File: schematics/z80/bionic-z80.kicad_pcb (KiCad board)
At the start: 2 copper layers, 27.9 x 68.6 mm, 8 parts, among them J1 Bionic-P135, J2 Bionic-P245, U1 Z84C00, U2 11AA010-I/TT

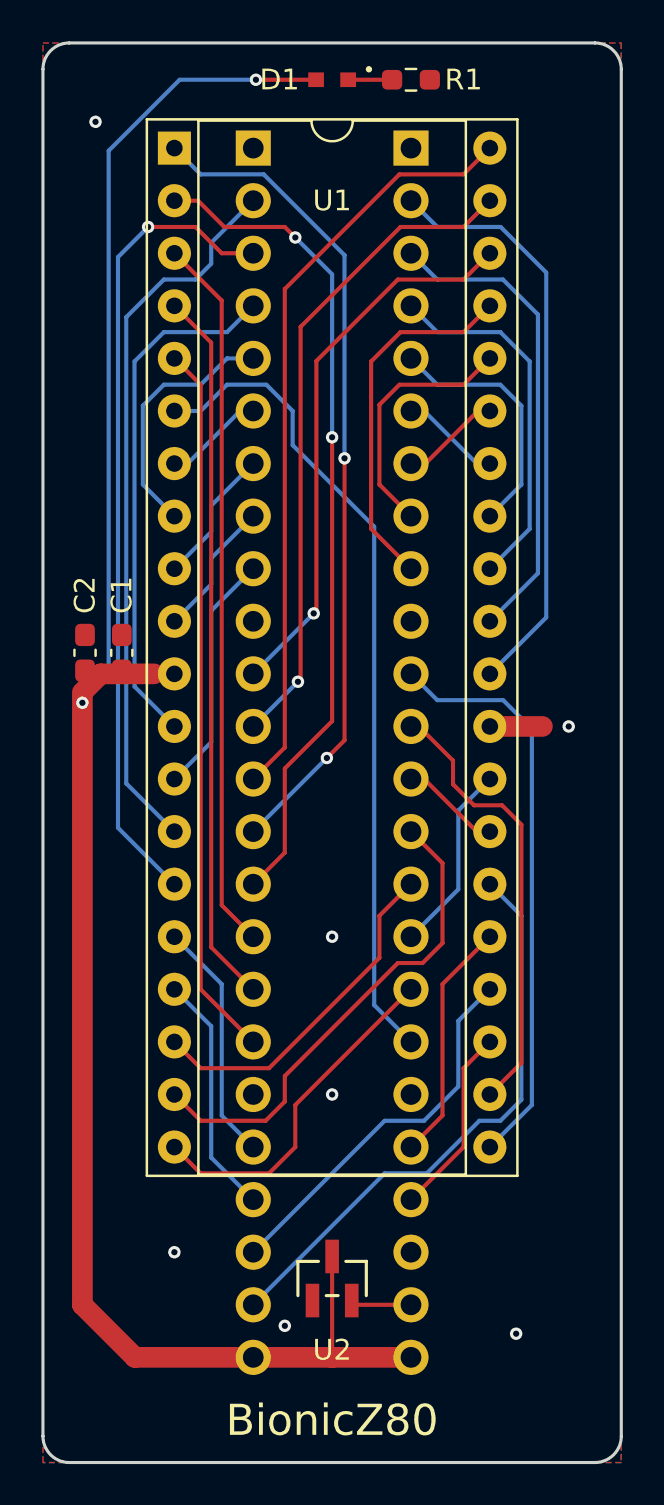
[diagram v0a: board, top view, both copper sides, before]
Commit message: [Z80] Fix EEPROM pinout
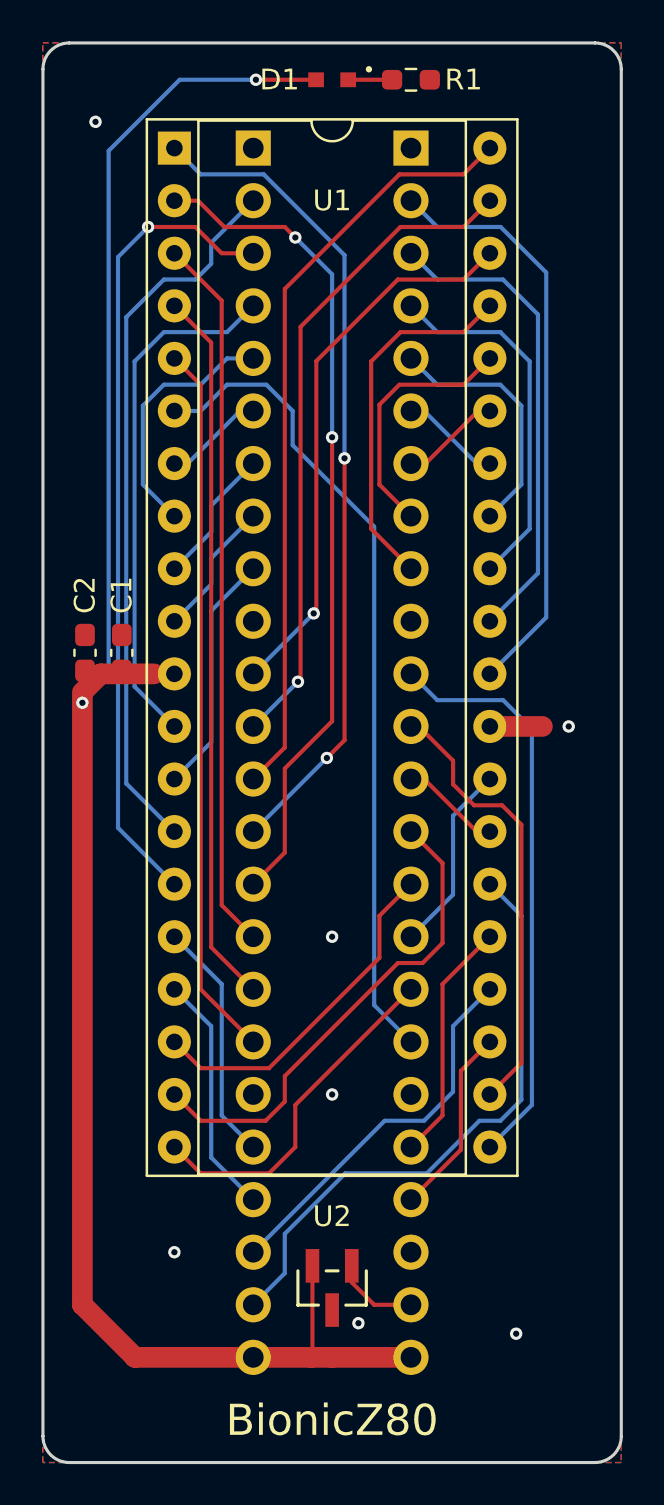
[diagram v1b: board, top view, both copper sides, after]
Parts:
- moved U2 0.46 mm to (115.0, 130.1), turned to 180 degrees
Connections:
- U2 pad 1: GND -> Net-(J2-P57)
- U2 pad 2: Net-(J2-P57) -> VCC
- U2 pad 3: VCC -> GND
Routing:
- net Net-(J2-P57): track 2.66 -> 4.10 mm
- net /P53: track 28.1 -> 29.2 mm
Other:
- board text added: "Rev. 3"
- board text removed: "Rev. 2"
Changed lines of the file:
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@@
   (title_block
     (title "BionicZ80")
-    (date "2024-05-25")
-    (rev "2")
+    (date "2024-11-02")
+    (rev "3")
     (company "Tadashi G. Takaoka")
   )
@@
   )
   (footprint "0-LocalLibrary:SOT-23_MC_MCH-M" (layer "F.Cu")
-    (at 114.97 129.69)
+    (at 114.97 130.148 180)
     (descr "Microchip 11AAxxx-I/TT UNI/O 1Kbit Serial EEPROM")
     (property "Sheetfile" "bionic-z80.kicad_sch")
@@
         (effects (font (size 1 1) (thickness 0.15)))
     )
-    (fp_text value "11AA010-I/TT" (at 0 0 unlocked) (layer "F.Fab")
+    (fp_text value "11AA010-I/TT" (at 0 0 180 unlocked) (layer "F.Fab")
         (effects (font (size 1 1) (thickness 0.15)))
     )
-    (fp_text user "${REFERENCE}" (at 0 0 unlocked) (layer "F.Fab")
+    (fp_text user "${REFERENCE}" (at 0 0 180 unlocked) (layer "F.Fab")
         (effects (font (size 1 1) (thickness 0.15)))
     )
@@
     (fp_circle (center -1.270999 0.446) (end -1.143999 0.446)
       (stroke (width 0.0254) (type solid)) (fill none) (layer "F.Fab"))
-    (pad "1" smd rect (at -0.950001 1.066) (size 0.6604 1.6256) (layers "F.Cu" "F.Paste" "F.Mask")
+    (pad "1" smd rect (at -0.950001 1.066 180) (size 0.6604 1.6256) (layers "F.Cu" "F.Paste" "F.Mask")
+      (net 44 "Net-(J2-P57)") (pinfunction "SCIO") (pintype "bidirectional"))
+    (pad "2" smd rect (at 0.950001 1.066 180) (size 0.6604 1.6256) (layers "F.Cu" "F.Paste" "F.Mask")
+      (net 1 "VCC") (pinfunction "VCC") (pintype "power_in"))
+    (pad "3" smd rect (at 0 -1.066 180) (size 0.6604 1.6256) (layers "F.Cu" "F.Paste" "F.Mask")
       (net 2 "GND") (pinfunction "VSS") (pintype "power_in"))
-    (pad "2" smd rect (at 0.950001 1.066) (size 0.6604 1.6256) (layers "F.Cu" "F.Paste" "F.Mask")
-      (net 44 "Net-(J2-P57)") (pinfunction "SCIO") (pintype "bidirectional"))
-    (pad "3" smd rect (at 0 -1.066) (size 0.6604 1.6256) (layers "F.Cu" "F.Paste" "F.Mask")
-      (net 1 "VCC") (pinfunction "VCC") (pintype "power_in"))
     (model "${KIPRJMOD}/0-LocalLibrary/SOT-23_MC_MCH.step"
       (offset (xyz 0 0 0))
@@
     (effects (font (size 0.8 0.8)) (justify bottom mirror))
   )
-  (gr_text "Rev. 2" (at 107.096 137.437) (layer "B.SilkS")
+  (gr_text "Rev. 3" (at 107.096 137.437) (layer "B.SilkS")
     (effects (font (size 1 1)) (justify left bottom mirror))
   )
@@
   )
   (segment (start 114.1953 71.778) (end 111.287 71.778) (width 0.2) (layer "F.Cu") (net 1))
-  (segment locked (start 114.97 133.5) (end 114.97 128.624) (width 0.2) (layer "F.Cu") (net 1))
-  (segment locked (start 114.97 133.5) (end 111.16 133.5) (width 1) (layer "F.Cu") (net 1))
+  (segment (start 114.019999 133.434001) (end 113.954 133.5) (width 0.2) (layer "F.Cu") (net 1))
   (segment locked (start 103.794 100.48) (end 104.9635 100.48) (width 1) (layer "F.Cu") (net 1))
   (segment locked (start 104.9635 100.48) (end 106.368 100.48) (width 1) (layer "F.Cu") (net 1))
   (segment locked (start 102.905 130.96) (end 102.905 101.369) (width 1) (layer "F.Cu") (net 1))
+  (segment (start 114.019999 129.082) (end 114.019999 133.434001) (width 0.2) (layer "F.Cu") (net 1))
   (segment locked (start 103.032 101.242) (end 103.794 100.48) (width 1) (layer "F.Cu") (net 1))
+  (segment (start 114.97 133.5) (end 113.954 133.5) (width 1) (layer "F.Cu") (net 1))
   (segment locked (start 105.445 133.5) (end 102.905 130.96) (width 1) (layer "F.Cu") (net 1))
   (segment locked (start 118.78 133.5) (end 114.97 133.5) (width 1) (layer "F.Cu") (net 1))
   (segment locked (start 111.16 133.5) (end 105.445 133.5) (width 1) (layer "F.Cu") (net 1))
+  (segment (start 113.954 133.5) (end 111.16 133.5) (width 1) (layer "F.Cu") (net 1))
   (via (at 111.287 71.778) (size 0.6) (drill 0.3) (layers "F.Cu" "B.Cu") (net 1))
   (via (at 102.905 101.877) (size 0.6) (drill 0.3) (layers "F.Cu" "B.Cu") (net 1))
@@
   (via (at 114.97 113.18) (size 0.6) (drill 0.3) (layers "F.Cu" "B.Cu") (free) (net 2))
   (via (at 123.86 132.357) (size 0.6) (drill 0.3) (layers "F.Cu" "B.Cu") (free) (net 2))
-  (via (at 112.684 131.976) (size 0.6) (drill 0.3) (layers "F.Cu" "B.Cu") (free) (net 2))
+  (via (at 116.24 131.849) (size 0.6) (drill 0.3) (layers "F.Cu" "B.Cu") (free) (net 2))
   (via (at 107.35 128.42) (size 0.6) (drill 0.3) (layers "F.Cu" "B.Cu") (free) (net 2))
+  (segment (start 124.114 112.164) (end 122.59 110.64) (width 0.2) (layer "B.Cu") (net 3))
+  (segment (start 115.605 124.61) (end 119.542 124.61) (width 0.2) (layer "B.Cu") (net 3))
+  (segment (start 111.16 130.96) (end 112.684 129.436) (width 0.2) (layer "B.Cu") (net 3))
+  (segment (start 112.684 129.436) (end 112.684 127.531) (width 0.2) (layer "B.Cu") (net 3))
+  (segment (start 123.098 122.07) (end 124.114 121.054) (width 0.2) (layer "B.Cu") (net 3))
+  (segment (start 119.542 124.61) (end 122.082 122.07) (width 0.2) (layer "B.Cu") (net 3))
+  (segment (start 122.082 122.07) (end 123.098 122.07) (width 0.2) (layer "B.Cu") (net 3))
   (segment (start 124.114 121.054) (end 124.114 112.164) (width 0.2) (layer "B.Cu") (net 3))
-  (segment (start 122.082 122.07) (end 123.098 122.07) (width 0.2) (layer "B.Cu") (net 3))
-  (segment (start 119.542 124.61) (end 122.082 122.07) (width 0.2) (layer "B.Cu") (net 3))
-  (segment (start 111.16 130.96) (end 117.51 124.61) (width 0.2) (layer "B.Cu") (net 3))
-  (segment (start 124.114 112.164) (end 122.59 110.64) (width 0.2) (layer "B.Cu") (net 3))
-  (segment (start 123.098 122.07) (end 124.114 121.054) (width 0.2) (layer "B.Cu") (net 3))
-  (segment (start 117.51 124.61) (end 119.542 124.61) (width 0.2) (layer "B.Cu") (net 3))
+  (segment (start 112.684 127.531) (end 115.605 124.61) (width 0.2) (layer "B.Cu") (net 3))
   (segment (start 117.256 87.474827) (end 117.256 91.336) (width 0.2) (layer "F.Cu") (net 5))
   (segment (start 121.32 86.51) (end 118.220827 86.51) (width 0.2) (layer "F.Cu") (net 5))
@@
   (segment (start 108.366 81.43) (end 109.128 80.668) (width 0.2) (layer "B.Cu") (net 28))
   (segment (start 105.026 83.246) (end 106.842 81.43) (width 0.2) (layer "B.Cu") (net 28))
-  (segment (start 121.066 107.084) (end 121.066 110.894) (width 0.2) (layer "B.Cu") (net 29))
-  (segment (start 122.59 105.56) (end 121.066 107.084) (width 0.2) (layer "B.Cu") (net 29))
-  (segment (start 121.066 110.894) (end 118.78 113.18) (width 0.2) (layer "B.Cu") (net 29))
+  (segment (start 120.812 111.148) (end 118.78 113.18) (width 0.2) (layer "B.Cu") (net 29))
+  (segment (start 122.59 105.56) (end 120.812 107.338) (width 0.2) (layer "B.Cu") (net 29))
+  (segment (start 120.812 107.338) (end 120.812 111.148) (width 0.2) (layer "B.Cu") (net 29))
   (segment (start 114.716 104.544) (end 115.57 103.69) (width 0.2) (layer "F.Cu") (net 30))
   (segment (start 115.57 103.69) (end 115.57 90.066) (width 0.2) (layer "F.Cu") (net 30))
@@
   (segment (start 107.35 115.72) (end 109.128 117.498) (width 0.2) (layer "B.Cu") (net 34))
   (segment (start 109.128 117.498) (end 109.128 123.848) (width 0.2) (layer "B.Cu") (net 34))
-  (segment (start 121.32 119.53) (end 122.59 118.26) (width 0.2) (layer "F.Cu") (net 35))
-  (segment (start 118.78 125.88) (end 121.32 123.34) (width 0.2) (layer "F.Cu") (net 35))
-  (segment (start 121.32 123.34) (end 121.32 119.53) (width 0.2) (layer "F.Cu") (net 35))
+  (segment (start 121.193 123.467) (end 121.193 119.657) (width 0.2) (layer "F.Cu") (net 35))
+  (segment (start 121.193 119.657) (end 122.59 118.26) (width 0.2) (layer "F.Cu") (net 35))
+  (segment (start 118.78 125.88) (end 121.193 123.467) (width 0.2) (layer "F.Cu") (net 35))
   (segment (start 118.78 108.1) (end 120.304 109.624) (width 0.2) (layer "F.Cu") (net 36))
   (segment (start 118.145 114.45) (end 112.684 119.911) (width 0.2) (layer "F.Cu") (net 36))
@@
   (segment (start 120.304 109.624) (end 120.304 113.485173) (width 0.2) (layer "F.Cu") (net 36))
   (segment (start 112.684 119.911) (end 112.684 121.142346) (width 0.2) (layer "F.Cu") (net 36))
-  (segment (start 121.066 117.244) (end 122.59 115.72) (width 0.2) (layer "B.Cu") (net 37))
+  (segment (start 120.812 117.498) (end 122.59 115.72) (width 0.2) (layer "B.Cu") (net 37))
+  (segment (start 120.812 120.673) (end 120.812 117.498) (width 0.2) (layer "B.Cu") (net 37))
   (segment (start 111.16 128.42) (end 117.51 122.07) (width 0.2) (layer "B.Cu") (net 37))
   (segment (start 117.51 122.07) (end 119.415 122.07) (width 0.2) (layer "B.Cu") (net 37))
-  (segment (start 121.066 120.419) (end 121.066 117.244) (width 0.2) (layer "B.Cu") (net 37))
-  (segment (start 119.415 122.07) (end 121.066 120.419) (width 0.2) (layer "B.Cu") (net 37))
+  (segment (start 119.415 122.07) (end 120.812 120.673) (width 0.2) (layer "B.Cu") (net 37))
   (segment (start 120.304 121.816) (end 118.78 123.34) (width 0.2) (layer "F.Cu") (net 38))
   (segment (start 122.59 113.18) (end 120.304 115.466) (width 0.2) (layer "F.Cu") (net 38))
@@
   (segment (start 123.232909 101.75) (end 120.05 101.75) (width 0.2) (layer "B.Cu") (net 42))
   (segment (start 120.05 101.75) (end 118.78 100.48) (width 0.2) (layer "B.Cu") (net 42))
-  (segment locked (start 118.78 130.96) (end 116.124 130.96) (width 0.2) (layer "F.Cu") (net 44))
+  (segment (start 117.002 130.96) (end 118.78 130.96) (width 0.2) (layer "F.Cu") (net 44))
+  (segment (start 115.920001 129.878001) (end 117.002 130.96) (width 0.2) (layer "F.Cu") (net 44))
+  (segment (start 115.920001 129.082) (end 115.920001 129.878001) (width 0.2) (layer "F.Cu") (net 44))
   (zone (net 2) (net_name "GND") (layers "F&B.Cu") (hatch edge 0.5)
     (connect_pads (clearance 0.35))

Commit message: [Z80] Shrink board size
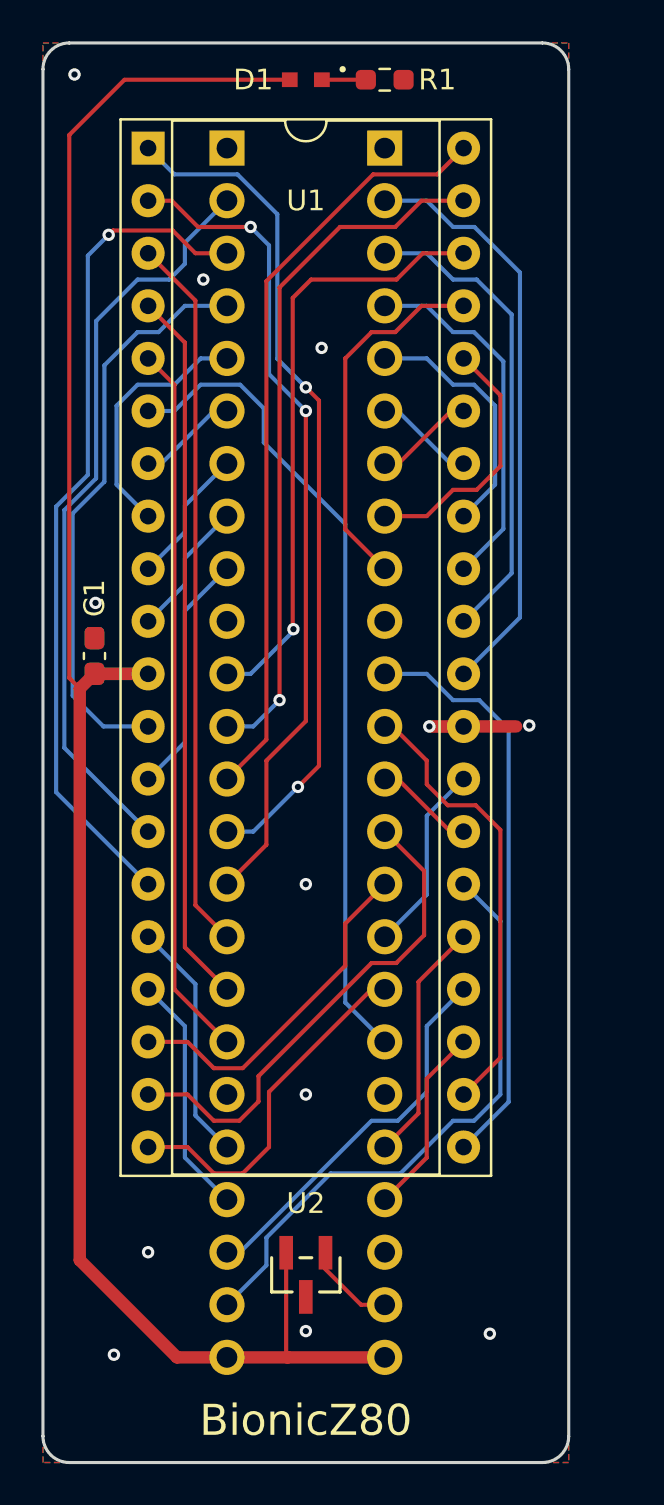
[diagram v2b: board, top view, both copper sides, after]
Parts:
- C2: moved to B.Cu
- moved U2 1.42 mm to (113.7, 129.5)
- moved C1 1.33 mm to (103.5, 99.6)
- moved D1 1.27 mm to (113.7, 71.8)
- moved J1 1.27 mm to (109.9, 75.1)
- moved J2 1.27 mm to (117.5, 75.1)
- moved R1 1.27 mm to (117.5, 71.8)
- moved U1 1.27 mm to (106.1, 75.1)
- moved C2 0.48 mm to (103.5, 99.6)
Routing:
- net GND: track 2.54 -> 5.84 mm, vias 7 -> 12
- net /P12: track 25.3 -> 28.0 mm
- net /P30: track 26.9 -> 29.3 mm
- net /P31: track 31.9 -> 33.6 mm
- net /P11: track 39.1 -> 40.5 mm
- net /P10: track 34.9 -> 36.3 mm
- net VCC: track 93.3 -> 94.3 mm, vias 2 -> 0
- net /P33: track 40.0 -> 40.8 mm
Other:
- board size 27.9 x 68.6 mm -> 25.4 x 68.6 mm

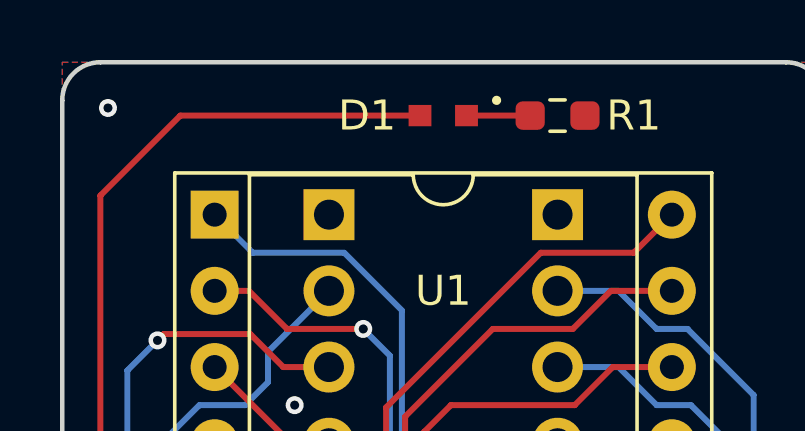
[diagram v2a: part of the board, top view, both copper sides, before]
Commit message: [schematics] Update LED footprint
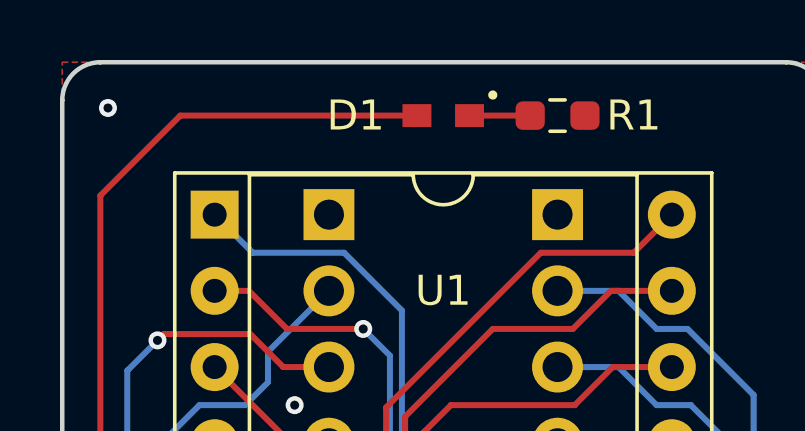
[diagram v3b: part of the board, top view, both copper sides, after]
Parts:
- D1: footprint 0-LocalLibrary:LED_CSL1901UW1_ROM -> 0-LocalLibrary:LED_CSL1901UW1_ROM-M
